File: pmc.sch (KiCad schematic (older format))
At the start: 167 parts, among them M1 TPS61040, M2 LM46001, M3 STM32F405RG, M4 REF3033, M5 TPS73633, M6 SN65HVD256, M7 UCC27211A, M8 UCC27211A, M9 UCC27211A, P1 FAN, P10 F1, P11 F2, P12 A1, P13 A2, P14 BOOT, P15 F1, P16 F2, P17 A1, P18 A2, P19 CONN4, P2 NTC, P20 CONN4, P21 CONN4, P22 CONN4, P23 CONN4, P3 HALL, P4 SPI, P5 PPM, P6 ANALOG, P7 CAN, P8 SWD, P9 USART, Q1 IRLML6401, Q2 IPT007N06N, Q3 IPT007N06N, Q4 IPT007N06N, Q5 IPT007N06N, Q6 IPT007N06N, Q7 IPT007N06N, U1 AD8539, U2 AD8539, U3 AD8417, U4 AD8417

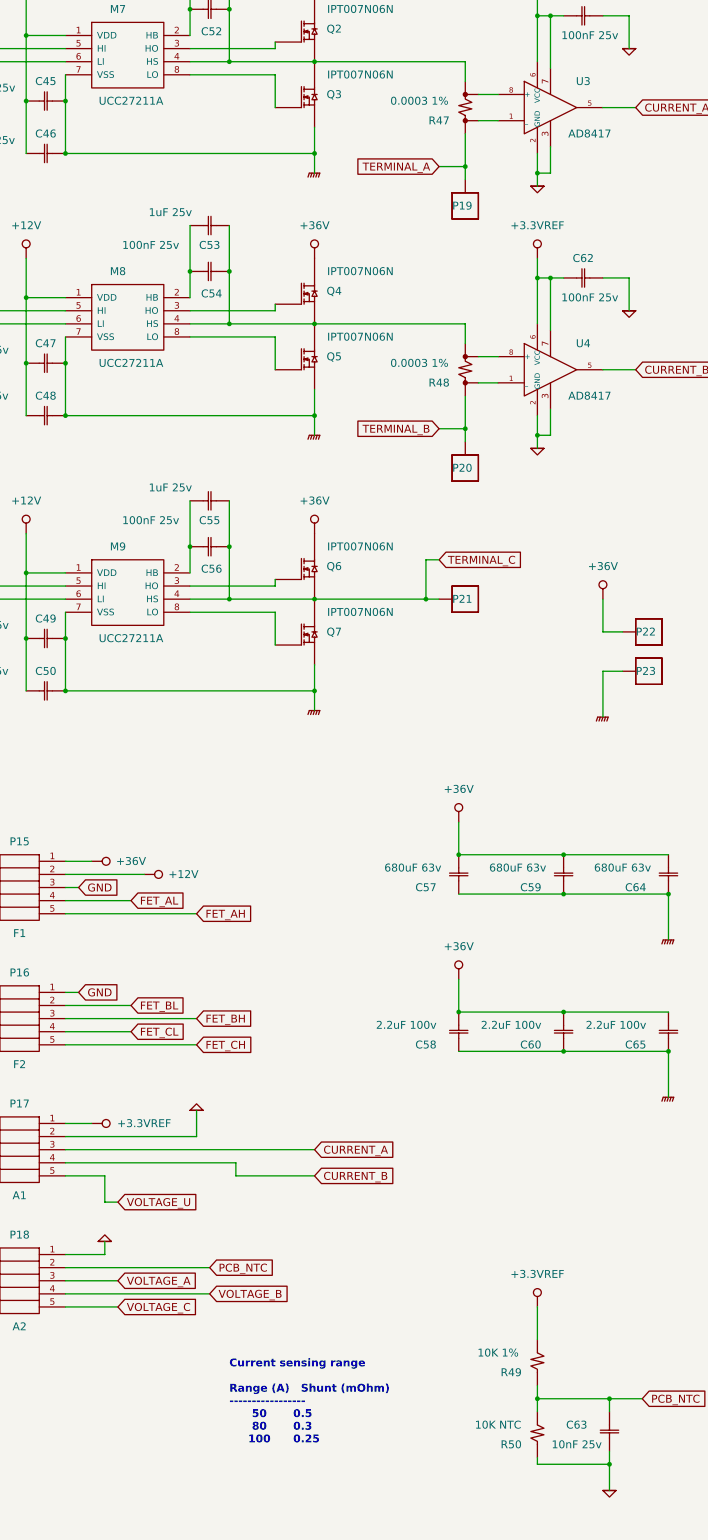
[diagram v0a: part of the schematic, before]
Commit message: New mosfet driver and current sensing amp.
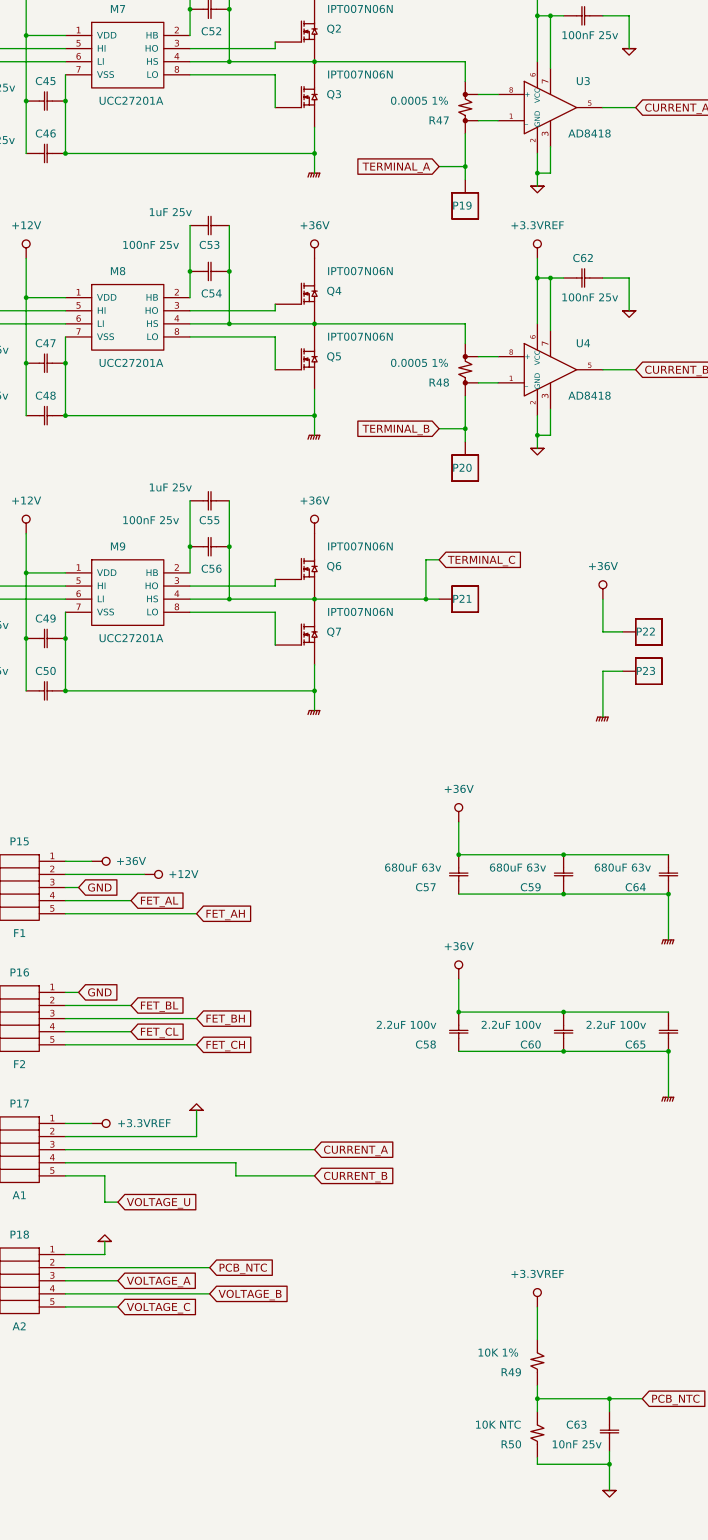
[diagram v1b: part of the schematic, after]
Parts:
- M7, M8, M9: value UCC27211A -> UCC27201A
- R47, R48: value 0.0003 1% -> 0.0005 1%
- U3, U4: value AD8417 -> AD8418
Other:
- note removed: "Current sensing range\n\nRange (A) Shunt (mOhm)\n-----------------\n 50 0.5\n 80 0.3\n 100 0.25"
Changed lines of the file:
@@
 Sheet 1 1
 Title "Phobia Motor Controller"
-Date "2019-04-27"
+Date "2019-06-02"
 Rev "4c"
 Comp "Roman Belov"
@@
 P 21100 2450
 F 0 "U3" H 21350 2650 60  0000 C CNN
-F 1 "AD8417" H 21400 2250 60  0000 C CNN
+F 1 "AD8418" H 21400 2250 60  0000 C CNN
 F 2 "foot:MSOP-8" H 21100 2450 60  0001 C CNN
 F 3 "" H 21100 2450 60  0000 C CNN
@@
 P 21100 4450
 F 0 "U4" H 21350 4650 60  0000 C CNN
-F 1 "AD8417" H 21400 4250 60  0000 C CNN
+F 1 "AD8418" H 21400 4250 60  0000 C CNN
 F 2 "foot:MSOP-8" H 21100 4450 60  0001 C CNN
 F 3 "" H 21100 4450 60  0000 C CNN
@@
 P 17900 2050
 F 0 "M7" H 17800 2400 60  0000 C CNN
-F 1 "UCC27211A" H 17900 1700 60  0000 C CNN
+F 1 "UCC27201A" H 17900 1700 60  0000 C CNN
 F 2 "foot:SON-8" H 17500 1700 60  0001 C CNN
 F 3 "" H 17900 2050 60  0000 C CNN
@@
 P 17900 4050
 F 0 "M8" H 17800 4400 60  0000 C CNN
-F 1 "UCC27211A" H 17900 3700 60  0000 C CNN
+F 1 "UCC27201A" H 17900 3700 60  0000 C CNN
 F 2 "foot:SON-8" H 17500 3700 60  0001 C CNN
 F 3 "" H 17900 4050 60  0000 C CNN
@@
 P 17900 6150
 F 0 "M9" H 17800 6500 60  0000 C CNN
-F 1 "UCC27211A" H 17900 5800 60  0000 C CNN
+F 1 "UCC27201A" H 17900 5800 60  0000 C CNN
 F 2 "foot:SON-8" H 17500 5800 60  0001 C CNN
 F 3 "" H 17900 6150 60  0000 C CNN
@@
 P 20450 2450
 F 0 "R47" V 20350 2650 60  0000 C CNN
-F 1 "0.0003 1%" V 20500 2800 60  0000 C CNN
+F 1 "0.0005 1%" V 20500 2800 60  0000 C CNN
 F 2 "foot:LR2512-4" H 20450 2450 60  0001 C CNN
 F 3 "" H 20450 2450 60  0000 C CNN
@@
 P 20450 4450
 F 0 "R48" V 20350 4650 60  0000 C CNN
-F 1 "0.0003 1%" V 20500 4800 60  0000 C CNN
+F 1 "0.0005 1%" V 20500 4800 60  0000 C CNN
 F 2 "foot:LR2512-4" H 20450 4450 60  0001 C CNN
 F 3 "" H 20450 4450 60  0000 C CNN
@@
 	-1   0    0    1
 $EndComp
-Text Notes 18650 12650 0    60   ~ 12
-Current sensing range\n\nRange (A)   Shunt (mOhm)\n-----------------\n      50       0.5\n      80       0.3\n     100      0.25
 Text Notes 10500 3550 0    60   ~ 12
 R33 is not fitted\n

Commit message: Two analog channels.
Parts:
- removed P6: ANALOG, foot:PLS-3, symbol PLS_3
- removed P9: USART, foot:PLS-4, symbol PLS_4
- added C67: 10nF 25v, foot:SM-0603, symbol C
- added P6: ANALOG, foot:PLS-4, symbol PLS_4
- added P9: USART, foot:PLS-3, symbol PLS_3
- added R53, R54: 10K 1%, foot:SM-0603, symbol R
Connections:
- net +3.3V: now also P9.1
- net +5V: now also P6.1
- net ADC_IN14: now also C67.2, R53.2, R54.1; no longer C40.2, R34.2, R36.1
- net AGND: now also C67.1, P6.4, R53.1
- net USART_RX: now also P9.3
- net USART_TX: now also P9.2
- net ADC_IN9: now reaches M3.27 (PB1/ADC_IN9)
- net ADC_IN9: now also C40.2, R34.2, R36.1
- net at R36.2: now also P6.2
- new net: P6.3, R54.2
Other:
- note added: "Analog control input\nBrake input\n5v supply ouput"
- note removed: "Analog control input\n5v supply ouput"
- moved on the sheet: C35, C36, C40, C66, M6, P14, P4, P5, P7, P8, R34, R35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
